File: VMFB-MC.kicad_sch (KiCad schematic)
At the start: 51 parts, among them J1 DISPENSE, J10 PIR, J2 EMPTY, J3 DISPENSE, J4 DEPOSIT, J5 Conn_01x03_Pin, J6 DISPENSE, J7 EMPTY, J8 MOTOR, J9 Conn_01x10_Pin, Q1 Q_Photo_NPN, Q10 Q_Photo_NPN, Q2 Q_Photo_NPN, Q3 Q_Photo_NPN, Q4 Q_Photo_NPN, Q5 Q_Photo_NPN, Q6 Q_Photo_NPN, Q7 TIP120, Q8 TIP120, Q9 BC337, U1 LM393

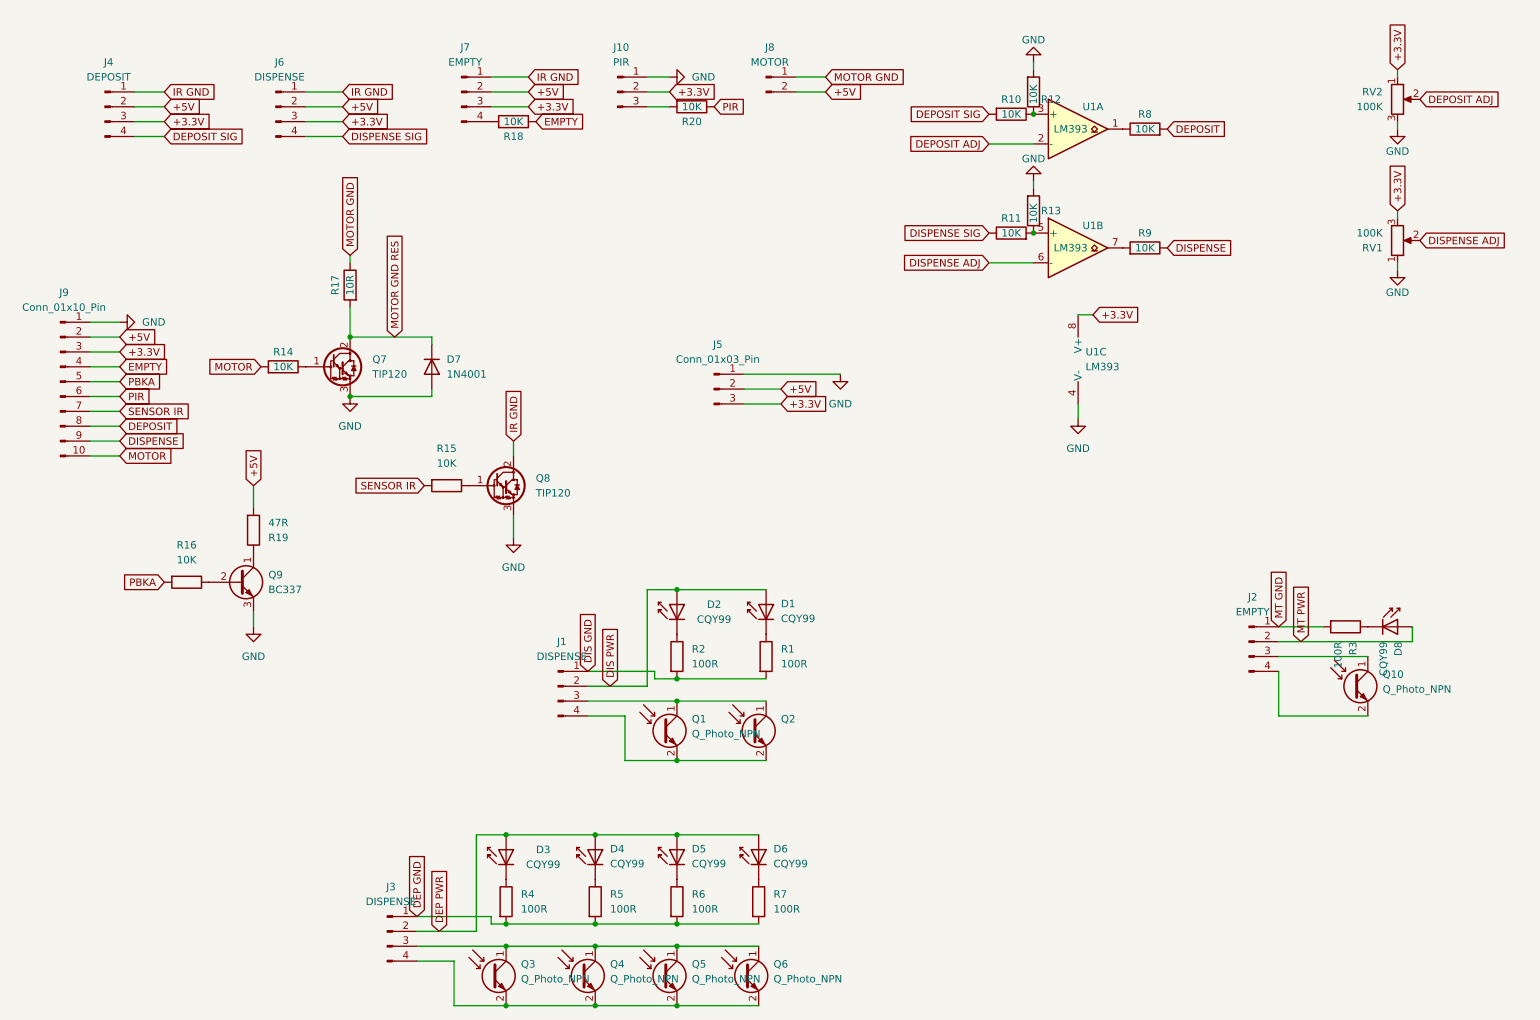
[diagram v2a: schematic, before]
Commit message: layout update
updates layout to compress it a bit.
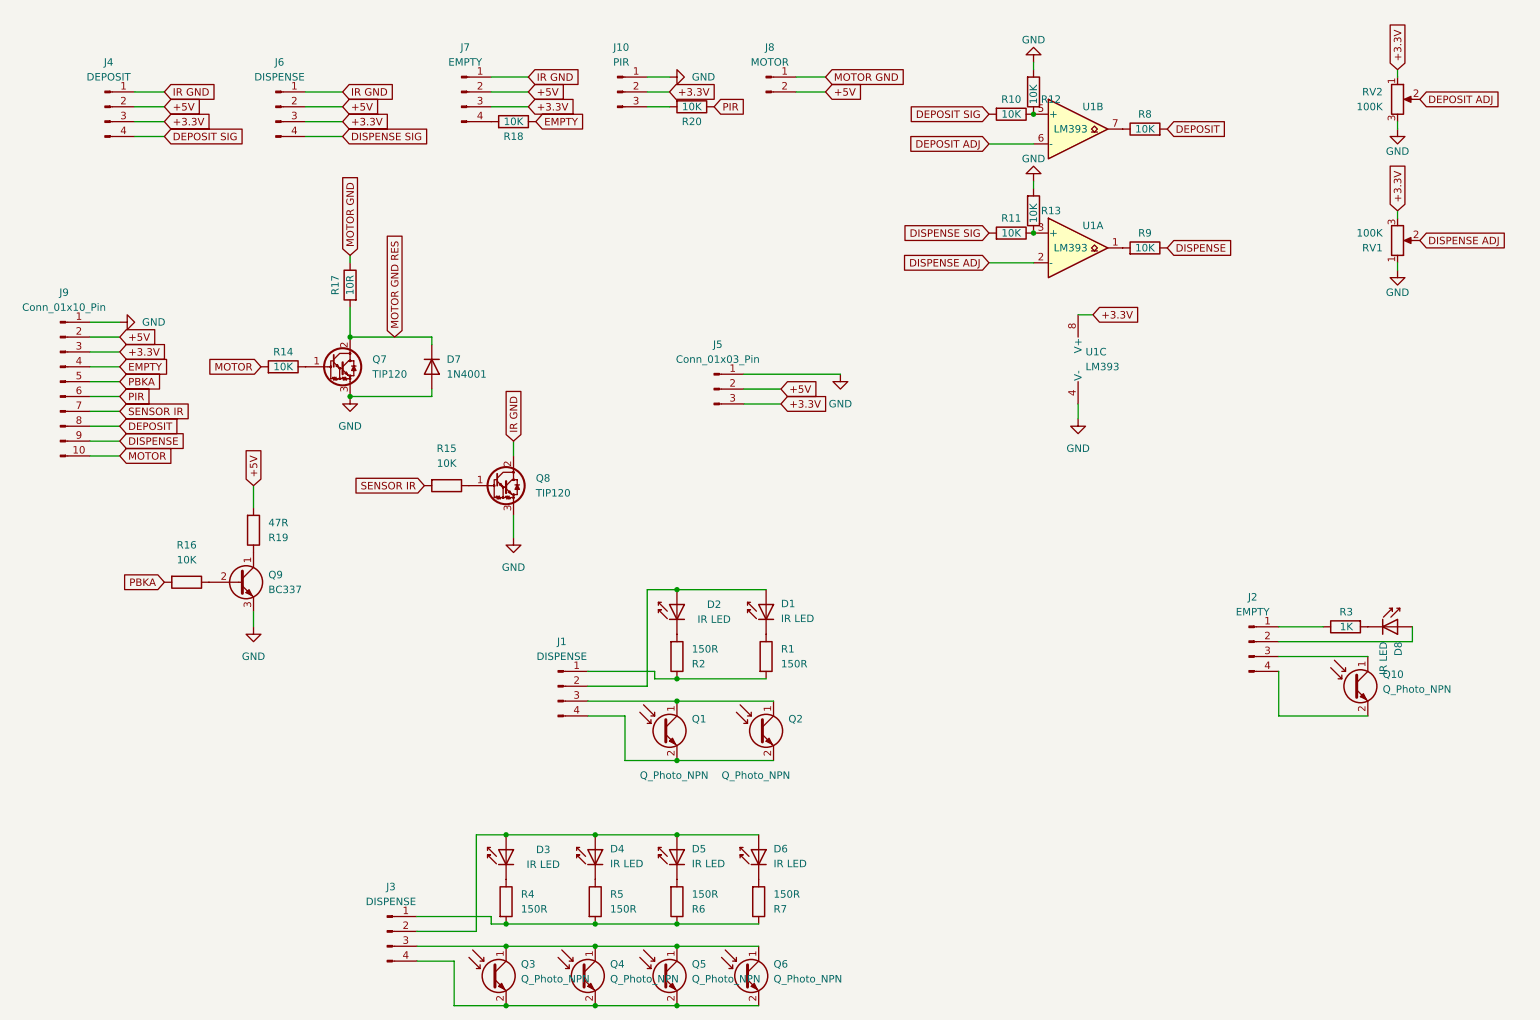
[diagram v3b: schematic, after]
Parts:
- D1, D2, D3, D4, D5, D6, D8: value CQY99 -> IR LED
- R1, R2, R4, R5, R6, R7: value 100R -> 150R
- R3: value 100R -> 1K
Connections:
- net DEPOSIT ADJ: now also U1.6 (-); no longer U1.2 (-)
- net DISPENSE ADJ: now also U1.2 (-); no longer U1.6 (-)
- net DISPENSE SIG: now also R11.2; no longer R11.1
- net at U1.1: now also R9.2; no longer R8.1
- net at R10.1, R12.1: now also U1.5 (+); no longer U1.3 (+)
- net at U1.7: now also R8.1; no longer R9.2
- net at R3.1: now also J2.1 (Pin_1); no longer D8.1 (K)
- net at R7.1: now also J3.1 (Pin_1), R4.2, R5.2, R6.1; no longer D6.1 (K)
- net at D5.1 (K): now also R6.2; no longer R6.1
- net at R2.1: now also J1.1 (Pin_1), R1.2; no longer D2.1 (K)
- removed net DEP GND: J3.1 (Pin_1), R4.2, R5.2, R6.2, R7.2
- net DEP PWR: no longer names the net of D3.2 (A), D4.2 (A), D5.2 (A), D6.2 (A), J3.2 (Pin_2)
- removed net DIS GND: J1.1 (Pin_1), R1.2, R2.2
- net DIS PWR: no longer names the net of D1.2 (A), D2.2 (A), J1.2 (Pin_2)
- net MT GND: no longer names the net of R3.2
- net MT GND: now also D8.1 (K); no longer J2.1 (Pin_1)
- net MT PWR: no longer names the net of D8.2 (A), J2.2 (Pin_2)
- new net: R11.1, R13.1, U1.3 (+)
- new net: D6.1 (K), R7.2
- new net: D2.1 (K), R2.2
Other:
- moved on the sheet: Q2, R11, R3, U1A, U1B

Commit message: Layout tweaks
more layout and labelling tweaks
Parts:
- RV1, RV2: footprint Potentiometer_THT:Potentiometer_Piher_PT-15-V02_Vertical -> Potentiometer_THT:Potentiometer_Piher_PT-10-V10_Vertical
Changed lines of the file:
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@@
       (effects (font (size 1.27 1.27)) (justify right))
     )
-    (property "Footprint" "Potentiometer_THT:Potentiometer_Piher_PT-15-V02_Vertical" (at 251.46 35.56 0)
+    (property "Footprint" "Potentiometer_THT:Potentiometer_Piher_PT-10-V10_Vertical" (at 251.46 35.56 0)
       (effects (font (size 1.27 1.27)) hide)
     )
@@
       (effects (font (size 1.27 1.27)) (justify right))
     )
-    (property "Footprint" "Potentiometer_THT:Potentiometer_Piher_PT-15-V02_Vertical" (at 251.46 59.69 0)
-      (effects (font (size 1.27 1.27)) hide)
-    )
+    (property "Footprint" "Potentiometer_THT:Potentiometer_Piher_PT-10-V10_Vertical" (at 251.46 59.69 0)
+      (effects (font (size 1.27 1.27)) hide)
+    )
